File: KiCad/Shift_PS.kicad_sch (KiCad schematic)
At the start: 40 parts

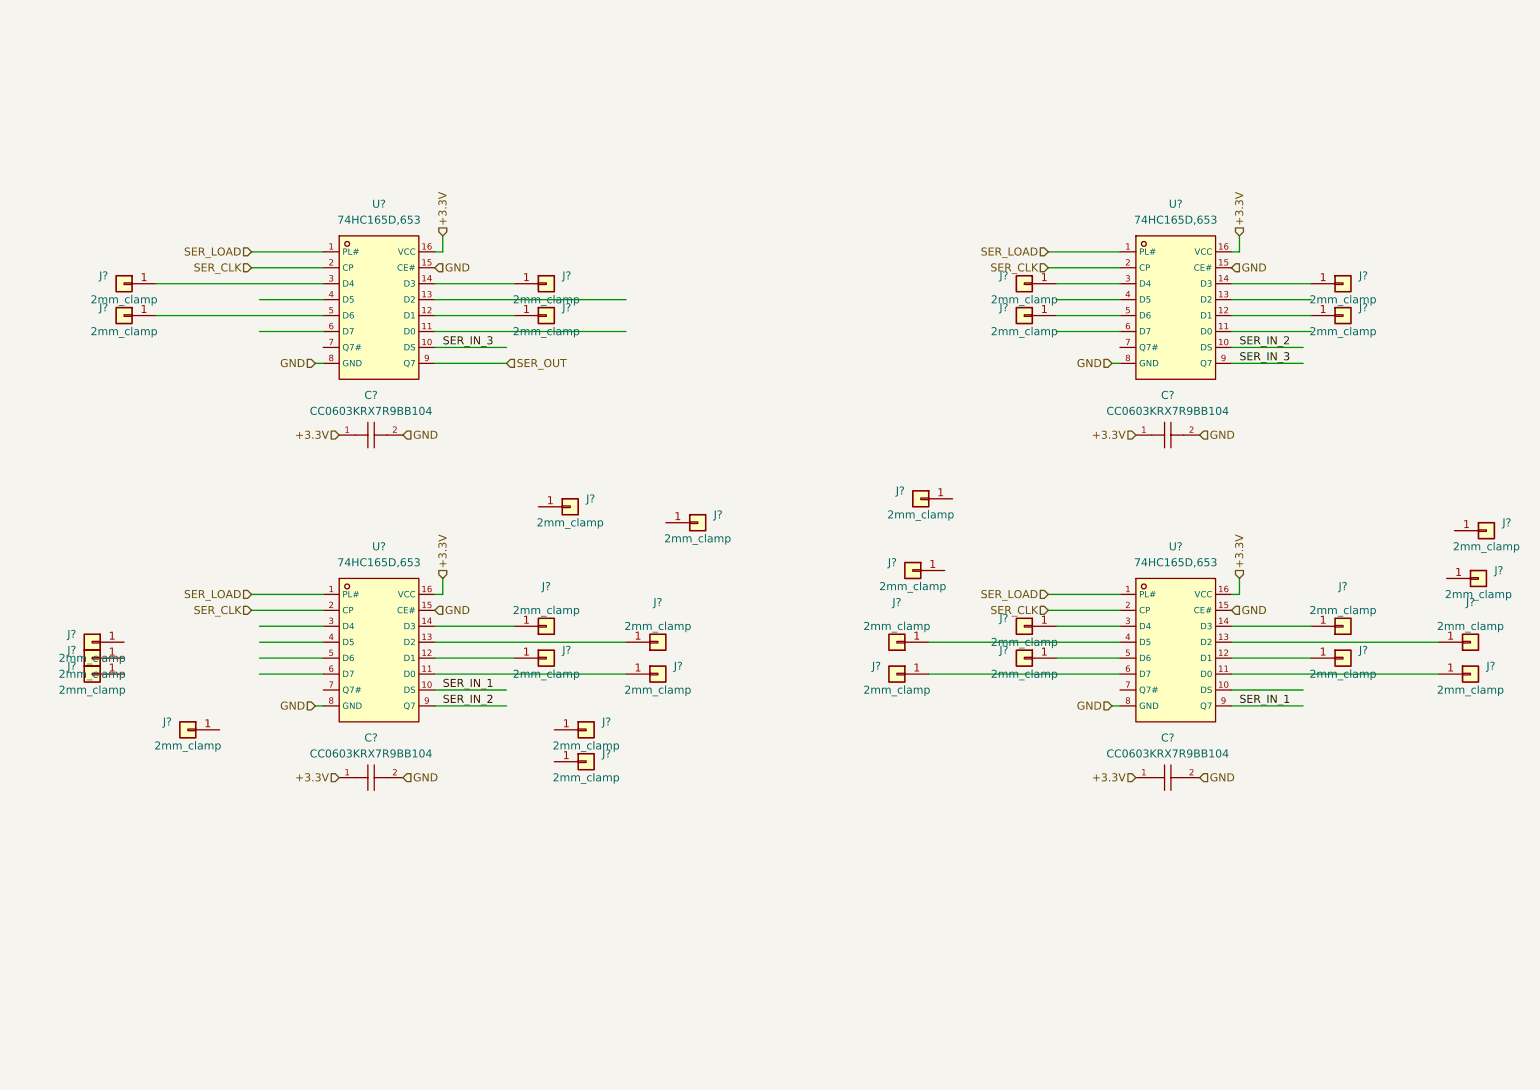
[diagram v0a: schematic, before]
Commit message: Update to TOP pcb - 2mm holes placement and routing
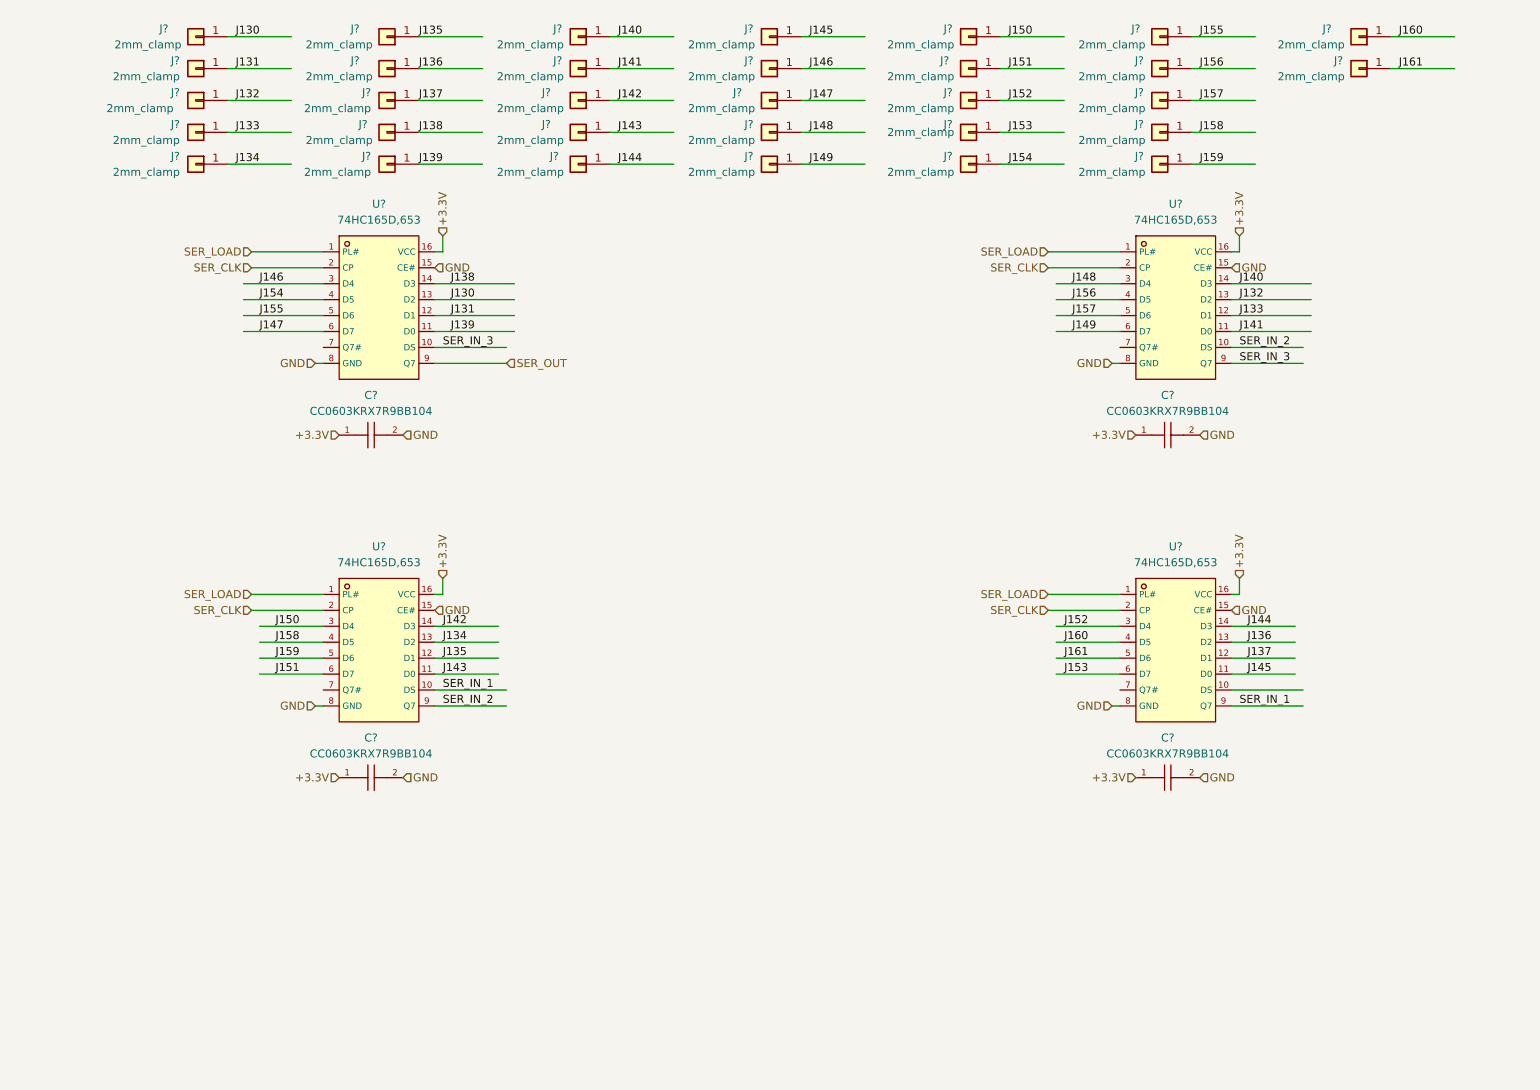
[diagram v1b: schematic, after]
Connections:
- net J154: now reaches J?.1 (Pin_1)
- net J154: now also U?.4 (D5)
- net J147: now reaches J?.1 (Pin_1)
- net J147: now also U?.6 (D7)
- net J135: now reaches J?.1 (Pin_1), U?.12 (D1)
- net J130: now reaches J?.1 (Pin_1)
- net J130: now also U?.13 (D2); no longer U?.3 (D4)
- net J141: now reaches U?.11 (D0)
- net J141: now also J?.1 (Pin_1)
- net J133: now reaches U?.12 (D1)
- net J133: now also J?.1 (Pin_1); no longer J?.1 (Pin_1)
- net J132: now reaches U?.13 (D2)
- net J132: now also J?.1 (Pin_1)
- net J140: now reaches U?.14 (D3)
- net J140: now also J?.1 (Pin_1); no longer J?.1 (Pin_1)
- net J148: now reaches U?.3 (D4)
- net J148: now also J?.1 (Pin_1); no longer J?.1 (Pin_1)
- net J156: now reaches U?.4 (D5)
- net J156: now also J?.1 (Pin_1)
- net J157: now reaches U?.5 (D6)
- net J157: now also J?.1 (Pin_1); no longer J?.1 (Pin_1)
- net J149: now reaches U?.6 (D7)
- net J149: now also J?.1 (Pin_1)
- net J143: now reaches J?.1 (Pin_1), U?.11 (D0)
- net J134: now reaches J?.1 (Pin_1), U?.13 (D2)
- net J142: now reaches J?.1 (Pin_1), U?.14 (D3)
- net J150: now reaches U?.3 (D4)
- net J150: now also J?.1 (Pin_1)
- net J158: now reaches U?.4 (D5)
- net J158: now also J?.1 (Pin_1)
- net J159: now reaches U?.5 (D6)
- net J159: now also J?.1 (Pin_1)
- net J151: now reaches U?.6 (D7)
- net J151: now also J?.1 (Pin_1)
- net J161: now reaches J?.1 (Pin_1), U?.5 (D6)
- net J137: now reaches J?.1 (Pin_1), U?.12 (D1)
- net J131: now reaches U?.12 (D1)
- net J131: now also J?.1 (Pin_1); no longer J?.1 (Pin_1)
- net J144: now reaches J?.1 (Pin_1), U?.14 (D3)
- net J138: now reaches J?.1 (Pin_1)
- net J138: now also U?.14 (D3); no longer U?.5 (D6)
- net J152: now reaches J?.1 (Pin_1), U?.3 (D4)
- net J145: now reaches J?.1 (Pin_1), U?.11 (D0)
- net J136: now reaches J?.1 (Pin_1), U?.13 (D2)
- net J160: now reaches J?.1 (Pin_1), U?.4 (D5)
- net J153: now reaches J?.1 (Pin_1), U?.6 (D7)
- net J155: now reaches J?.1 (Pin_1)
- net J155: now also U?.5 (D6)
- net J146: now reaches J?.1 (Pin_1)
- net J146: now also U?.3 (D4)
- net J139: now reaches U?.11 (D0)
- net J139: now also J?.1 (Pin_1)
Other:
- moved on the sheet: J?

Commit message: Ready for review
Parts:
- removed J? (x3): 2mm_clamp, Kaboom_box:2mm testlead, screw-clamp, symbol Kaboom_box:2mm_clamp
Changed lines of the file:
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@@
-    (stroke (width 0) (type default))
-  )
-  (wire (pts (xy 234.95 24.13) (xy 245.11 24.13))
     (stroke (width 0) (type default))
   )
@@
     (stroke (width 0) (type default))
   )
-  (wire (pts (xy 203.2 44.45) (xy 213.36 44.45))
-    (stroke (width 0) (type default))
-  )
   (wire (pts (xy 82.55 123.19) (xy 92.71 123.19))
     (stroke (width 0) (type default))
@@
     (stroke (width 0) (type default))
   )
-  (wire (pts (xy 234.95 29.21) (xy 245.11 29.21))
-    (stroke (width 0) (type default))
-  )
   (wire (pts (xy 49.53 29.21) (xy 59.69 29.21))
     (stroke (width 0) (type default))
@@
     (effects (font (size 1.27 1.27)) (justify left bottom))
   )
-  (label "J160" (at 236.22 24.13 0) (fields_autoplaced)
-    (effects (font (size 1.27 1.27)) (justify left bottom))
-  )
   (label "SER_IN_1" (at 210.82 130.81 0) (fields_autoplaced)
     (effects (font (size 1.27 1.27)) (justify left bottom))
@@
     (effects (font (size 1.27 1.27)) (justify left bottom))
   )
-  (label "J159" (at 204.47 44.45 0) (fields_autoplaced)
-    (effects (font (size 1.27 1.27)) (justify left bottom))
-  )
   (label "J148" (at 184.15 63.5 0) (fields_autoplaced)
     (effects (font (size 1.27 1.27)) (justify left bottom))
@@
   )
   (label "J150" (at 173.99 24.13 0) (fields_autoplaced)
-    (effects (font (size 1.27 1.27)) (justify left bottom))
-  )
-  (label "J161" (at 236.22 29.21 0) (fields_autoplaced)
     (effects (font (size 1.27 1.27)) (justify left bottom))
   )
@@
     )
   )
-  (symbol (lib_id "Kaboom_box:2mm_clamp") (at 229.87 29.21 0) (mirror y) (unit 1)
-    (in_bom yes) (on_board yes) (dnp no)
-    (property "Reference" "J?" (at 227.33 27.94 0)
-      (effects (font (size 1.27 1.27)) (justify left))
-    )
-    (property "Value" "2mm_clamp" (at 222.25 30.48 0)
-      (effects (font (size 1.27 1.27)))
-    )
-    (property "Footprint" "Kaboom_box:2mm testlead, screw-clamp" (at 231.14 34.29 0)
-      (effects (font (size 1.27 1.27)) hide)
-    )
-    (property "Datasheet" "https://www.aliexpress.com/item/1005003745780405.html?spm=a2g0o.order_list.order_list_main.12.1f5c18020OVUCx" (at 232.41 36.83 0)
-      (effects (font (size 1.27 1.27)) hide)
-    )
-    (pin "1")
-    (instances
-      (project "Kaboom_box"
-        (path "/8d340784-229e-46d1-990c-7f8852f9fc49"
-          (reference "J?") (unit 1)
-        )
-        (path "/8d340784-229e-46d1-990c-7f8852f9fc49/d111de2c-3c3c-486e-8c4b-bd3963817676"
-          (reference "J?") (unit 1)
-        )
-        (path "/8d340784-229e-46d1-990c-7f8852f9fc49/d111de2c-3c3c-486e-8c4b-bd3963817676/919d5153-67ff-4420-984f-74490b836c87"
-          (reference "J?") (unit 1)
-        )
-        (path "/8d340784-229e-46d1-990c-7f8852f9fc49/c9ccc42e-41d9-40f0-918f-9c4b4cc23369/b91a06cc-d8a4-43a7-b652-a0f7f13c3d33"
-          (reference "J161") (unit 1)
-        )
-      )
-    )
-  )
   (symbol (lib_id "Kaboom_box:2mm_clamp") (at 74.93 34.29 0) (mirror y) (unit 1)
     (in_bom yes) (on_board yes) (dnp no)
@@
         (path "/8d340784-229e-46d1-990c-7f8852f9fc49/c9ccc42e-41d9-40f0-918f-9c4b4cc23369/b91a06cc-d8a4-43a7-b652-a0f7f13c3d33"
           (reference "J152") (unit 1)
-        )
-      )
-    )
-  )
-  (symbol (lib_id "Kaboom_box:2mm_clamp") (at 198.12 44.45 0) (mirror y) (unit 1)
-    (in_bom yes) (on_board yes) (dnp no)
-    (property "Reference" "J?" (at 195.58 43.18 0)
-      (effects (font (size 1.27 1.27)) (justify left))
-    )
-    (property "Value" "2mm_clamp" (at 190.5 45.72 0)
-      (effects (font (size 1.27 1.27)))
-    )
-    (property "Footprint" "Kaboom_box:2mm testlead, screw-clamp" (at 199.39 49.53 0)
-      (effects (font (size 1.27 1.27)) hide)
-    )
-    (property "Datasheet" "https://www.aliexpress.com/item/1005003745780405.html?spm=a2g0o.order_list.order_list_main.12.1f5c18020OVUCx" (at 200.66 52.07 0)
-      (effects (font (size 1.27 1.27)) hide)
-    )
-    (pin "1")
-    (instances
-      (project "Kaboom_box"
-        (path "/8d340784-229e-46d1-990c-7f8852f9fc49"
-          (reference "J?") (unit 1)
-        )
-        (path "/8d340784-229e-46d1-990c-7f8852f9fc49/d111de2c-3c3c-486e-8c4b-bd3963817676"
-          (reference "J?") (unit 1)
-        )
-        (path "/8d340784-229e-46d1-990c-7f8852f9fc49/d111de2c-3c3c-486e-8c4b-bd3963817676/919d5153-67ff-4420-984f-74490b836c87"
-          (reference "J?") (unit 1)
-        )
-        (path "/8d340784-229e-46d1-990c-7f8852f9fc49/c9ccc42e-41d9-40f0-918f-9c4b4cc23369/b91a06cc-d8a4-43a7-b652-a0f7f13c3d33"
-          (reference "J159") (unit 1)
         )
       )
@@
         )
       )
-    )
-  )
-  (symbol (lib_id "Kaboom_box:2mm_clamp") (at 229.87 24.13 180) (unit 1)
-    (in_bom yes) (on_board yes) (dnp no)
-    (property "Reference" "J?" (at 224.79 22.86 0)
-      (effects (font (size 1.27 1.27)))
-    )
-    (property "Value" "2mm_clamp" (at 222.25 25.4 0)
-      (effects (font (size 1.27 1.27)))
-    )
-    (property "Footprint" "Kaboom_box:2mm testlead, screw-clamp" (at 231.14 19.05 0)
-      (effects (font (size 1.27 1.27)) hide)
-    )
-    (property "Datasheet" "https://www.aliexpress.com/item/1005003745780405.html?spm=a2g0o.order_list.order_list_main.12.1f5c18020OVUCx" (at 232.41 16.51 0)
-      (effects (font (size 1.27 1.27)) hide)
-    )
-    (pin "1")
-    (instances
-      (project "Kaboom_box"
-        (path "/8d340784-229e-46d1-990c-7f8852f9fc49"
-          (reference "J?") (unit 1)
-        )
-        (path "/8d340784-229e-46d1-990c-7f8852f9fc49/d111de2c-3c3c-486e-8c4b-bd3963817676"
-          (reference "J?") (unit 1)
-        )
-        (path "/8d340784-229e-46d1-990c-7f8852f9fc49/d111de2c-3c3c-486e-8c4b-bd3963817676/919d5153-67ff-4420-984f-74490b836c87"
-          (reference "J?") (unit 1)
-        )
-        (path "/8d340784-229e-46d1-990c-7f8852f9fc49/c9ccc42e-41d9-40f0-918f-9c4b4cc23369/b91a06cc-d8a4-43a7-b652-a0f7f13c3d33"
-          (reference "J160") (unit 1)
-        )
-      )
